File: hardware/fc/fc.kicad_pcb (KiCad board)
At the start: 6 copper layers, 35 x 35 mm, 95 parts, among them J1 USB4110-GF-A, J2 Micro_SD_Card_Det1, J3 FROM_ESC, J4 CAM, J5 CAM_CC, J6 ELRS, J7 VTX, SW1 Push, U1 TPS7A8101DRBR, U10 TPS2116DRL, U11 OPA354AIDBVR, U12 RP2354A, U2 TPS7A8101DRBR, U3 LMR51420YFDDCR, U4 USBLC6-2SC6, U5 EMIF06-MSD02N16, U6 LSM6DSK320X, U8 TS5A3159ADCK, U9 TLV7031DCKR, X1 ABM8-272-T3

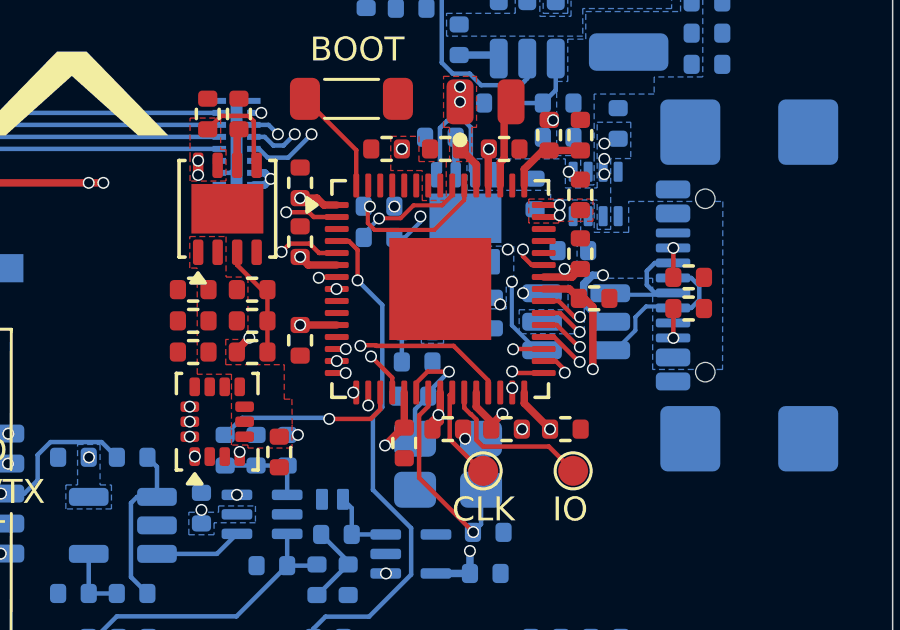
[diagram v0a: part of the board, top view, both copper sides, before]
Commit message: fc: add dshot resistors
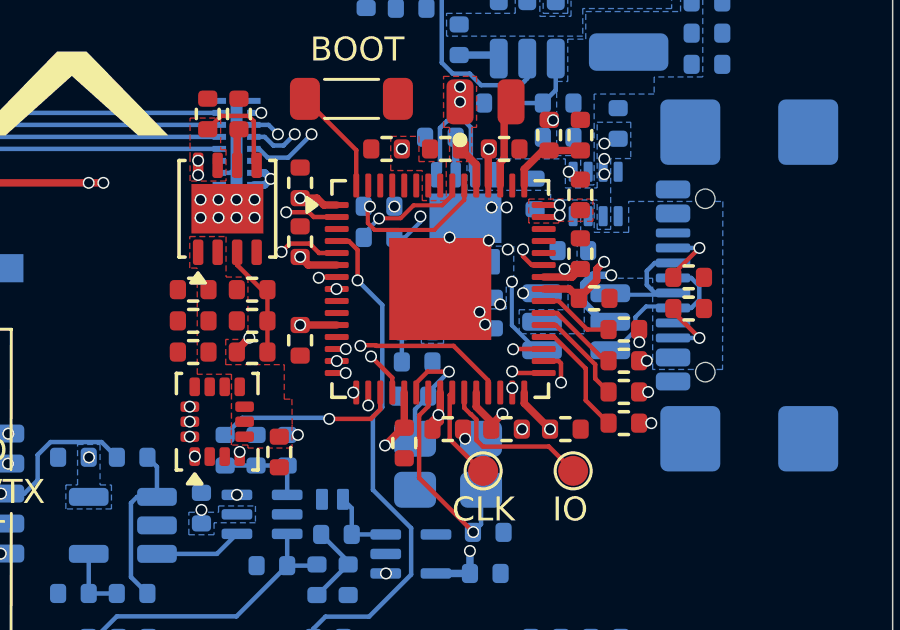
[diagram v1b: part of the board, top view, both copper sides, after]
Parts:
- added R22: 27R, Stratus:R_0402, F.Cu at (171.5, 115.2)
- added R23: 27R, Stratus:R_0402, F.Cu at (171.5, 114.1)
- added R24: 27R, Stratus:R_0402, F.Cu at (171.5, 112.1)
- added R25: 27R, Stratus:R_0402, F.Cu at (171.5, 113.1)
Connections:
- U12 pad 34: /Peripherals/ESC.M1 -> Net-(U12-GPIO22)
- U12 pad 35: /Peripherals/ESC.M2 -> Net-(U12-GPIO23)
- U12 pad 36: /Peripherals/ESC.M3 -> Net-(U12-GPIO24)
- U12 pad 37: /Peripherals/ESC.M4 -> Net-(U12-GPIO25)
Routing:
- net Net-(U12-GPIO22): track 0.00 -> 3.97 mm
- net Net-(U12-GPIO23): track 0.00 -> 3.36 mm
- net Net-(U12-GPIO24): track 0.00 -> 2.82 mm
- net Net-(U12-GPIO25): track 0.00 -> 2.55 mm
- net Net-(J1-CC2): track 0.98 -> 2.22 mm
- net Net-(J1-CC1): track 0.98 -> 2.22 mm
- net /Peripherals/ESC.M1: track 26.6 -> 27.8 mm
- net V_3V3: track 25.0 -> 24.3 mm
- net /Peripherals/ESC.M4: track 30.1 -> 30.7 mm
- net /Peripherals/SD.DAT0: track 15.9 -> 16.5 mm
- net /Peripherals/ESC.M2: track 27.4 -> 27.9 mm
- net GND: track 5.93 -> 6.22 mm, vias 32 -> 46

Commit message: fc: footprints
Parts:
- D1: footprint Diode_SMD:D_SOD-882 -> Stratus:D_0402
- H1, H2, H3, H4: footprint MountingHole:MountingHole_3.2mm_M3 -> Stratus:Mount_M3_K0.5
- U1, U2: footprint Package_SON:VSON-8-1EP_3x3mm_P0.65mm_EP1.65x2.4mm -> Stratus:TPS7A8101DRBR
- U10: footprint Package_TO_SOT_SMD:SOT-583-8 -> Stratus:TPS2116DRL
- U11: footprint Package_TO_SOT_SMD:SOT-23-5 -> Stratus:OPA354AIDBVR
- U12: footprint Package_DFN_QFN:QFN-60-1EP_7x7mm_P0.4mm_EP3.4x3.4mm -> Stratus:RP2354A
- U4: footprint Package_TO_SOT_SMD:SOT-23-6 -> Stratus:USBLC6-2SC6
- U6: footprint Package_LGA:LGA-14_3x2.5mm_P0.5mm_LayoutBorder3x4y -> Stratus:LSM6DSK320X
- U8: footprint Package_TO_SOT_SMD:SOT-363_SC-70-6 -> Stratus:TS5A3159ADCK
- U9: footprint Package_TO_SOT_SMD:SOT-353_SC-70-5 -> Stratus:TLV7031DCKR
- X1: footprint PCM_Crystal_AKL:Crystal_SMD_3225-4Pin_3.2x2.5mm -> Stratus:Crystal_4P_3.2x2.5mm
